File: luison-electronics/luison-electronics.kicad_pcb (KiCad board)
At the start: 2 copper layers, 120 x 80 mm, 28 parts, among them SW1 EECO_Micro-Dip_3500_B02, SW2 SW_Push, U1 YAAJ_DCDC_StepDown_LM2596

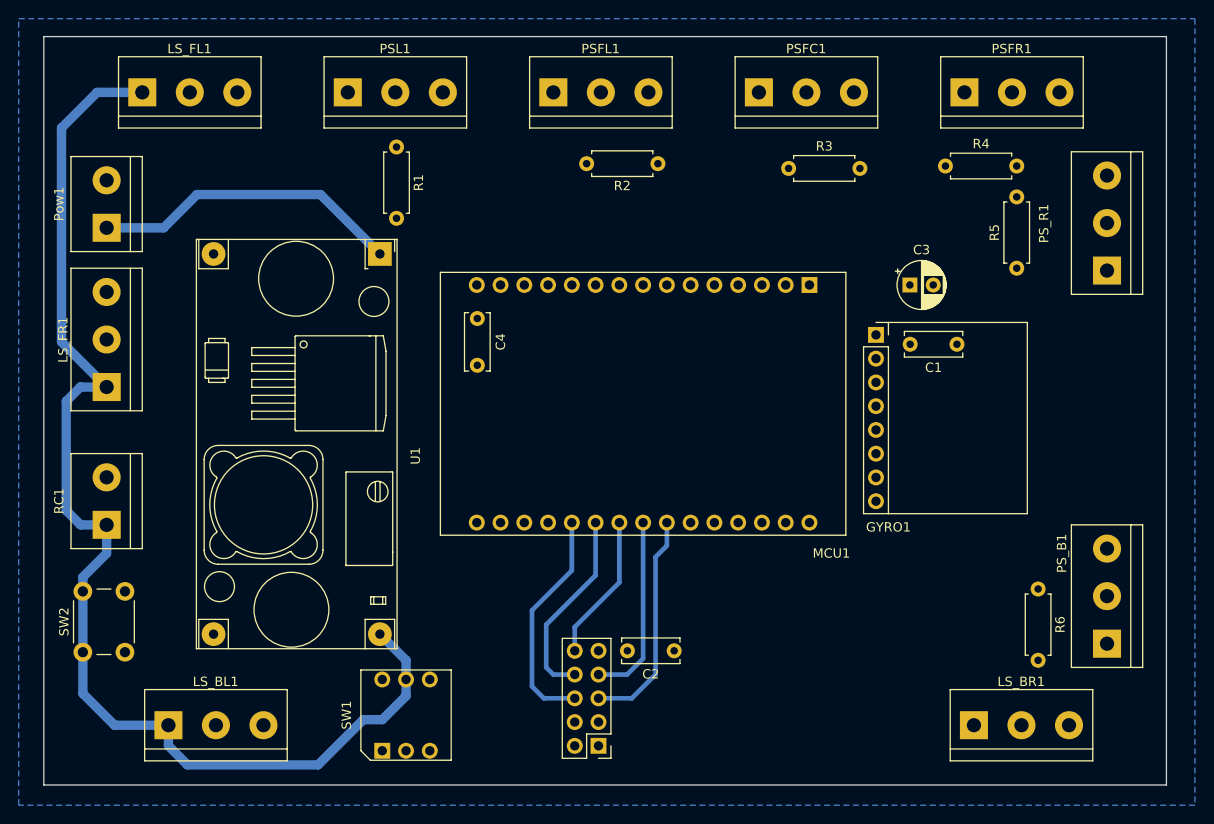
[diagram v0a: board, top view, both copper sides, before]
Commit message: Finish dual layer PCB and generate manufacture job files
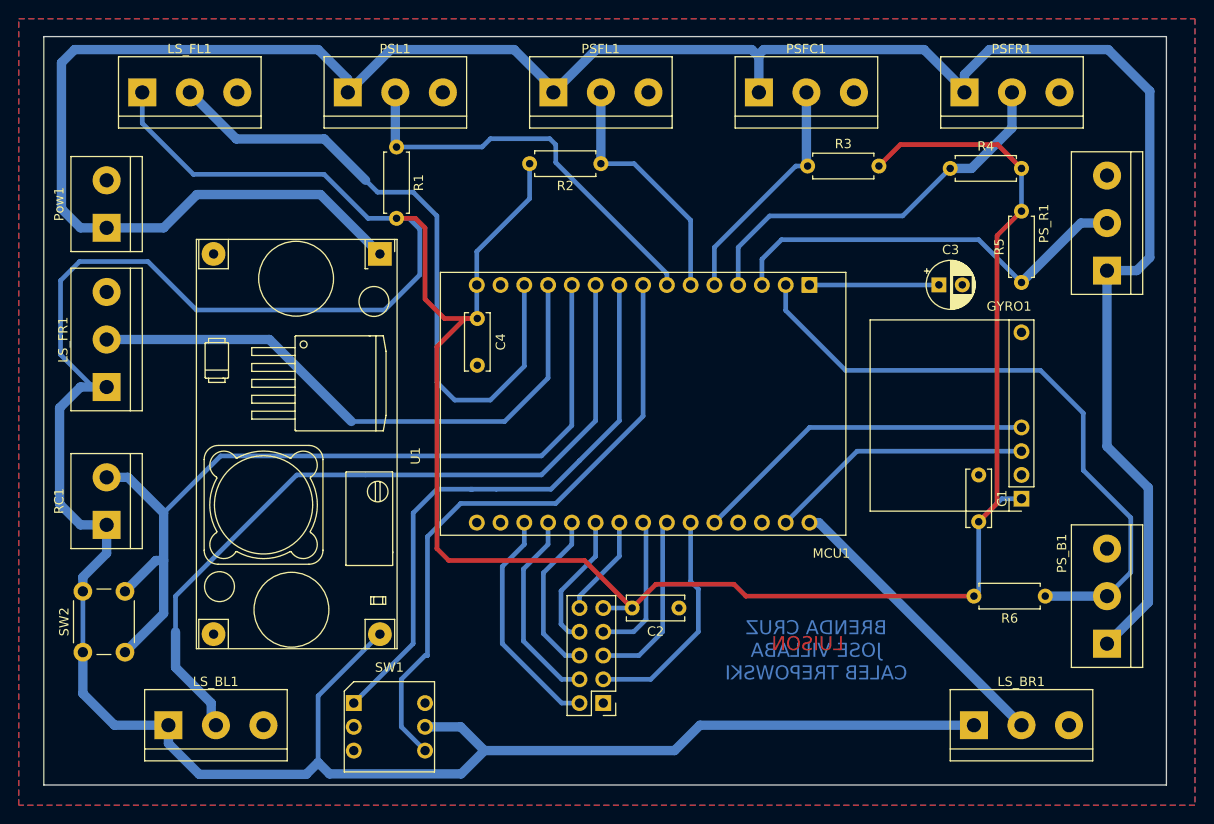
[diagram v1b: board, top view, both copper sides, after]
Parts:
- moved GYRO1 23.4 mm to (143.8, 122.9), turned to 180 degrees
- moved C1 14.2 mm to (139.2, 120.4), turned to -90 degrees
- moved R2 6.10 mm to (98.8, 87.1)
- moved SW1 5.94 mm to (72.4, 144.8), turned to -90 degrees
- moved C2 4.60 mm to (107.1, 134.6)
- moved MD1 4.60 mm to (99.1, 144.8)
- moved C3 3.11 mm to (134.9, 100.1)
- moved R3 2.05 mm to (120.9, 87.4)
- moved R5 1.61 mm to (143.8, 99.8)
- moved R6 1.08 mm to (146.3, 133.3), turned to 180 degrees
- moved R4 0.57 mm to (136.1, 87.6)
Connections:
- LS_BL1 pad 2: /GPIO14 -> /GPIO27
- LS_FR1 pad 2: /GPIO27 -> /GPIO12
- MCU1 pad 29: (no net) -> Net-(GYRO1-Pad3)
- Pow1 pad 2: (no net) -> GND
- RC1 pad 2: /GPIO12 -> /GPIO14
- SW2 pad 2: /GPIO12 -> /GPIO14
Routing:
- net +3.3V: track 130.4 -> 467.0 mm
- net +24V: track 33.3 -> 258.0 mm
- net /GPIO14: track 0.00 -> 92.3 mm
- net /GPIO27: track 0.00 -> 82.8 mm
- net /GPIO13: track 0.00 -> 70.0 mm
- net Net-(MCU1-Pad2): track 0.00 -> 68.4 mm
- net /GPIO25: track 0.00 -> 67.6 mm
- net /GPIO26: track 0.00 -> 63.8 mm
- net /GPIO12: track 0.00 -> 62.7 mm
- net Net-(MCU1-Pad3): track 0.00 -> 45.0 mm
- net Net-(MCU1-Pad7): track 0.00 -> 43.5 mm
- net Net-(MCU1-Pad4): track 0.00 -> 42.4 mm
- net Net-(GYRO1-Pad4): track 0.00 -> 37.0 mm
- net Net-(LS_BR1-Pad2): track 0.00 -> 31.6 mm
- net Net-(GYRO1-Pad3): track 0.00 -> 28.4 mm
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- added copper zone on F.Cu, net GND
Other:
- board text added: "BRENDA CRUZ JOSE VILLABA CALEB TREPOWSKI"
- board text added: "LUISON"

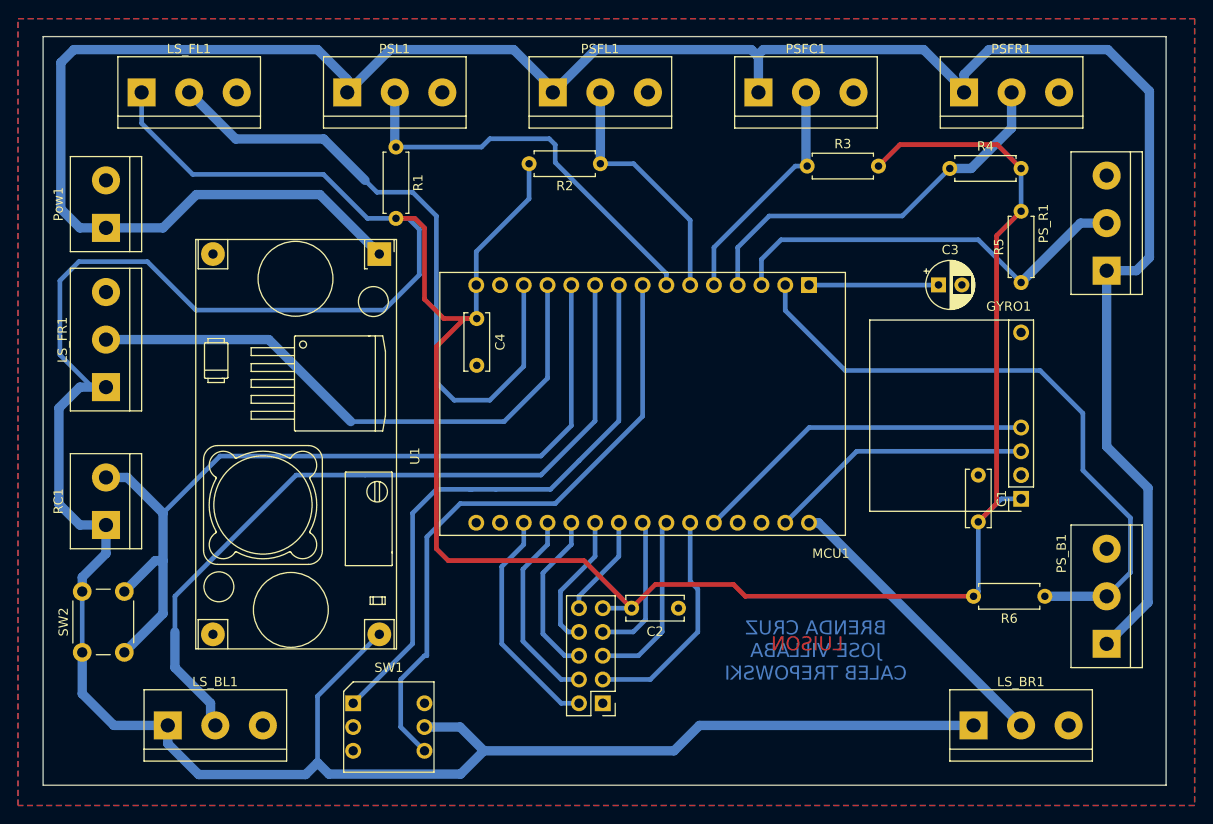
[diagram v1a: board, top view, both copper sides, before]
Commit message: Fix tracks, track widths and non-copper areas. Generate job files
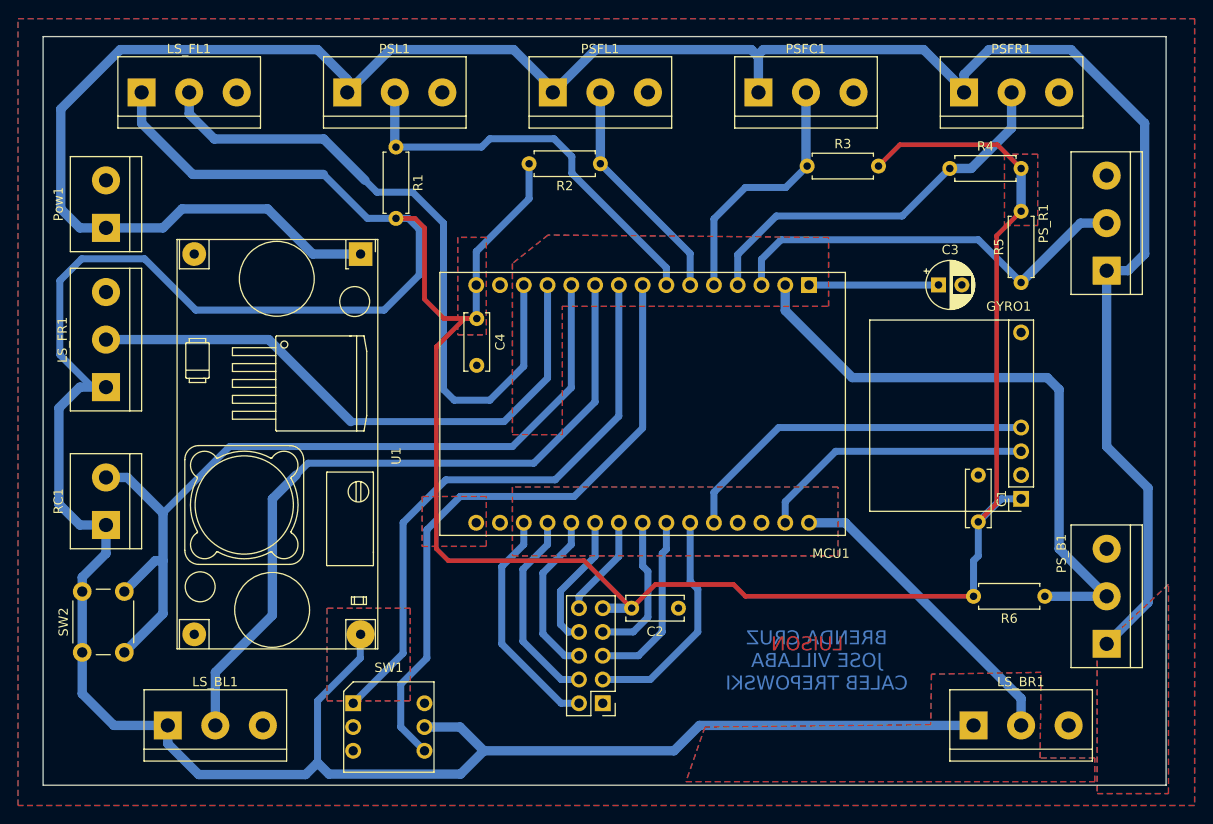
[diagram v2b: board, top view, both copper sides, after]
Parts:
- moved U1 2.00 mm to (73.2, 96.8)
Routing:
- net +24V: track 258.0 -> 248.6 mm
- net /GPIO27: track 82.8 -> 78.7 mm
- net /GPIO14: track 92.3 -> 89.9 mm
- net Net-(MCU1-Pad2): track 68.4 -> 66.3 mm
- net Net-(MCU1-Pad6): track 26.9 -> 24.8 mm
- net Net-(GYRO1-Pad4): track 37.0 -> 38.9 mm
- net Net-(MCU1-Pad5): track 25.5 -> 27.3 mm
- net Net-(LS_BR1-Pad2): track 31.6 -> 33.3 mm
- net /GPIO13: track 70.0 -> 71.3 mm
- net Net-(GYRO1-Pad3): track 28.4 -> 29.7 mm
- net /GPIO25: track 67.6 -> 68.7 mm
- net +3.3V: track 467.0 -> 466.4 mm
- net /GPIO26: track 63.8 -> 63.3 mm

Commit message: Add new symbols in schematic and new layout of pcb
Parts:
- added LS1: Line_Sensor, luison-electronics:JST_XH_B3B-XH-A_1x03_P2.50mm_Vertical, F.Cu at (236.0, 34.3)
- added LS2: Line_Sensor, luison-electronics:JST_XH_B3B-XH-A_1x03_P2.50mm_Vertical, F.Cu at (224.3, 34.3)
- added LS3: Line_Sensor, luison-electronics:JST_XH_B3B-XH-A_1x03_P2.50mm_Vertical, F.Cu at (242.8, 33.3)
- added LS4: Line_Sensor, luison-electronics:JST_XH_B3B-XH-A_1x03_P2.50mm_Vertical, F.Cu at (241.6, 79.0)
- added MCU2: ESP32-S2-DevKitC-1, luison-electronics:ESP32-S2-DevKitC-1, F.Cu at (233.4, 88.6)
- added PS1: Omron_E3Z-D62_2M, luison-electronics:JST_XH_B3B-XH-A_1x03_P2.50mm_Vertical, F.Cu at (281.9, 80.5)
- added PS2: Omron_E3Z-D62_2M, luison-electronics:JST_XH_B3B-XH-A_1x03_P2.50mm_Vertical, F.Cu at (298.5, 80.5)
- added PS3: Omron_E3Z-D62_2M, luison-electronics:JST_XH_B3B-XH-A_1x03_P2.50mm_Vertical, F.Cu at (208.5, 34.5)
- added PS4: Omron_E3Z-D62_2M, luison-electronics:JST_XH_B3B-XH-A_1x03_P2.50mm_Vertical, F.Cu at (229.4, 79.0)
- added PS5: Omron_E3Z-D62_2M, luison-electronics:JST_XH_B3B-XH-A_1x03_P2.50mm_Vertical, F.Cu at (205.3, 89.9)
- added PS6: Omron_E3Z-D62_2M, luison-electronics:JST_XH_B3B-XH-A_1x03_P2.50mm_Vertical, F.Cu at (298.5, 71.5)
- added REF**: MountingHole_3.2mm_M3, MountingHole:MountingHole_3.2mm_M3, F.Cu at (261.6, 27.7)
- added REF**: MountingHole_3.2mm_M3, MountingHole:MountingHole_3.2mm_M3, F.Cu at (261.6, 91.7)
- added REF**: MountingHole_3.2mm_M3, MountingHole:MountingHole_3.2mm_M3, F.Cu at (170.9, 91.7)
- added REF**: MountingHole_3.2mm_M3, MountingHole:MountingHole_3.2mm_M3, F.Cu at (170.9, 27.7)
- added SW3: EECO_Micro-Dip_3500_B02, luison-electronics:EECO Rotary Switch, F.Cu at (183.6, 84.6)
- moved C2 54.0 mm to (89.9, 83.4)
- moved GYRO1 54.0 mm to (126.5, 71.8)
- moved PS_B1 54.0 mm to (135.6, 87.2)
- moved SW2 54.0 mm to (26.2, 88.2)
- moved LS_FR1 54.0 mm to (28.7, 59.8)
- moved PS_R1 54.0 mm to (135.6, 47.4)
- moved Pow1 54.0 mm to (28.7, 42.8)
- moved R3 54.0 mm to (103.6, 36.2)
- moved R5 54.0 mm to (126.5, 48.6)
- moved C1 54.0 mm to (121.9, 69.2)
- moved C4 54.0 mm to (68.3, 52.5)
- moved LS_BL1 54.0 mm to (35.3, 96.0)
- moved LS_BR1 54.0 mm to (121.4, 96.0)
- moved LS_FL1 54.0 mm to (32.5, 28.3)
- moved MCU1 54.0 mm to (86.0, 61.6)
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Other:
- board size 120 x 80 mm -> 243.7 x 80 mm

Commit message: Add killlswitch library and layout pcb components
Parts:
- added D1: LED_RGB, LED_THT:LED_D5.0mm-4_RGB, F.Cu at (239.3, 105.4)
- added R7: 1k, Resistor_THT:R_Axial_DIN0207_L6.3mm_D2.5mm_P7.62mm_Horizontal, F.Cu at (224.0, 107.2)
- added R8: 1k, Resistor_THT:R_Axial_DIN0207_L6.3mm_D2.5mm_P7.62mm_Horizontal, F.Cu at (213.3, 111.2)
- added R9: 1k, Resistor_THT:R_Axial_DIN0207_L6.3mm_D2.5mm_P7.62mm_Horizontal, F.Cu at (213.3, 107.2)
- added U2: Robochallenge_KillSwitch, luison-electronics:Robochallenge_KillSwitch, F.Cu at (174.5, 71.9)
- moved PS1 86.2 mm to (195.8, 84.0), turned to 90 degrees
- moved PS2 64.5 mm to (244.6, 45.2), turned to 90 degrees
- moved MCU2 64.0 mm to (209.6, 29.2), turned to 0 degrees
- moved SW3 58.7 mm to (242.3, 86.9)
- moved PS6 56.1 mm to (246.1, 51.6), turned to -90 degrees
- moved PS5 48.8 mm to (246.1, 63.3), turned to -90 degrees
- moved LS2 47.7 mm to (195.6, 72.4), turned to 90 degrees
- moved LS3 47.5 mm to (195.6, 37.6), turned to 90 degrees
- moved LS4 45.8 mm to (244.6, 33.3), turned to 90 degrees
- moved LS1 43.0 mm to (195.6, 49.0), turned to 90 degrees
- moved PS3 29.0 mm to (195.8, 60.6), turned to 90 degrees
- moved REF** 17.5 mm to (188.5, 92.2)
- moved PS4 17.2 mm to (246.1, 75.0), turned to -90 degrees
- moved REF** 16.8 mm to (187.7, 27.7)
- moved REF** 5.59 mm to (256.0, 27.7)
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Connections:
- MCU2 pad 13: unconnected-(MCU2-Pad13) -> /KS_Start
- MCU2 pad 14: unconnected-(MCU2-Pad14) -> /KS_Em
- MCU2 pad 29: unconnected-(MCU2-Pad29) -> /LED_R
- MCU2 pad 30: unconnected-(MCU2-Pad30) -> /LED_G
- MCU2 pad 31: unconnected-(MCU2-Pad31) -> /LED_B
- MCU2 pad 32: unconnected-(MCU2-Pad32) -> /SW_P1
- MCU2 pad 33: unconnected-(MCU2-Pad33) -> /SW_P2
- MCU2 pad 34: unconnected-(MCU2-Pad34) -> /SW_P4
- MCU2 pad 35: unconnected-(MCU2-Pad35) -> /SW_P8
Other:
- board size 243.7 x 80 mm -> 241.2 x 80 mm

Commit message: Creacion de nueva placa
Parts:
- removed C1, C2, C4: 100nf, Capacitor_THT:C_Disc_D6.0mm_W2.5mm_P5.00mm
- removed C3: C, Capacitor_THT:CP_Radial_D5.0mm_P2.50mm
- removed D1: LED_RGB, LED_THT:LED_D5.0mm-4_RGB
- removed GYRO1: MPU-6050 Breakout Board, keilev_Library:MPU6050 Breakout Board
- removed LS_BL1, LS_BR1, LS_FL1, LS_FR1: Line_Sensor, TerminalBlock:TerminalBlock_bornier-3_P5.08mm
- removed MCU1: ESP32-Node32s, luison-electronics:ESP32-Node32s
- removed MD1: H-Bridge_Driver, Connector_PinHeader_2.54mm:PinHeader_2x05_P2.54mm_Vertical
- removed PSFC1, PSFL1, PSFR1, PSL1, PS_B1, PS_R1: Omron_E3Z-D62_2M, TerminalBlock:TerminalBlock_bornier-3_P5.08mm
- removed Pow1: Power_Supply, TerminalBlock:TerminalBlock_bornier-2_P5.08mm
- removed R1, R2, R3, R4, R5, R6: 1Meg, Resistor_THT:R_Axial_DIN0207_L6.3mm_D2.5mm_P7.62mm_Horizontal
- removed R7, R8, R9: 1k, Resistor_THT:R_Axial_DIN0207_L6.3mm_D2.5mm_P7.62mm_Horizontal
- removed RC1: Remote_Control_Module, TerminalBlock:TerminalBlock_bornier-2_P5.08mm
- removed SW1: EECO_Micro-Dip_3500_B02, luison-electronics:EECO Rotary Switch
- removed SW2: SW_Push, Button_Switch_THT:SW_PUSH_6mm
- removed U1: YAAJ_DCDC_StepDown_LM2596, luison-electronics:YAAJ_DCDC_StepDown_LM2596
- added ?: , , F.Cu at (170.8, 104.8)
- added ?: , , F.Cu at (179.1, 74.9)
- added ?: , , F.Cu at (138.4, 74.9)
- added ?: , , F.Cu at (123.6, 90.8)
- added GYRO2: MPU-6050 Breakout Board, luison-electronics:MPU6050 Breakout Board, F.Cu at (117.4, 82.5)
- added PS7: conector_driver, luison-electronics:JST_XH_B3B-XH-A_1x03_P2.50mm_Vertical, F.Cu at (148.0, 108.6)
- added PS8: alimentacion_driver, luison-electronics:JST_XH_B3B-XH-A_1x03_P2.50mm_Vertical, F.Cu at (115.4, 105.2)
- added PS9: alimentacion_driver, luison-electronics:JST_XH_B3B-XH-A_1x03_P2.50mm_Vertical, F.Cu at (115.3, 93.3)
- added REF**: custom_via, luison-electronics:custom_via, F.Cu at (141.6, 113.0)
- moved REF** 166.6 mm to (114.9, 116.2), turned to 0 degrees
- moved MCU2 110.6 mm to (127.0, 102.8), turned to 90 degrees
- moved LS4 107.9 mm to (143.5, 71.0), turned to 180 degrees
- moved PS2 94.4 mm to (175.8, 109.9), turned to 180 degrees
- moved LS1 92.3 mm to (125.1, 108.6), turned to 0 degrees
- moved SW3 87.2 mm to (156.2, 73.0), turned to 90 degrees
- moved PS4 79.9 mm to (166.4, 70.9), turned to 180 degrees
- moved REF** 79.2 mm to (114.9, 59.1), turned to 0 degrees
- moved PS5 73.7 mm to (172.7, 69.8), turned to 0 degrees
- moved REF** 72.7 mm to (190.5, 62.2), turned to 0 degrees
- moved LS3 71.8 mm to (132.0, 71.0), turned to 180 degrees
- moved LS2 69.2 mm to (136.6, 108.6), turned to 0 degrees
- moved PS6 60.1 mm to (189.2, 70.9), turned to 180 degrees
- moved PS3 49.8 mm to (182.2, 108.6), turned to 0 degrees
- moved U2 47.3 mm to (154.9, 114.9), turned to -90 degrees
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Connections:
- MCU2 pad 10: /TX1_MD -> /RX1_MD
- MCU2 pad 11: /RX1_MD -> /KS_START
- MCU2 pad 12: /SDA -> unconnected-(MCU2-IO8/ADC-Pad12)
- MCU2 pad 13: /KS_Start -> unconnected-(MCU2-IO3/ADC-Pad13)
- MCU2 pad 14: /KS_Em -> unconnected-(MCU2-I46-Pad14)
- MCU2 pad 15: /SCL -> /PS_FL
- MCU2 pad 17: /PS_FR -> unconnected-(MCU2-IO11/ADC-Pad17)
- MCU2 pad 18: /PS_FC -> unconnected-(MCU2-IO12/ADC-Pad18)
- MCU2 pad 19: /PS_FL -> /PS_FC
- MCU2 pad 20: unconnected-(MCU2-Pad20) -> /PS_FR
- MCU2 pad 24: unconnected-(MCU2-Pad24) -> /LS_FR
- MCU2 pad 25: unconnected-(MCU2-Pad25) -> /SDA
- MCU2 pad 26: /LS_BR -> /SCL
- MCU2 pad 27: /LS_BL -> unconnected-(MCU2-IO2/ADC-Pad27)
- MCU2 pad 28: unconnected-(MCU2-Pad28) -> /LS_BR
- MCU2 pad 29: /LED_R -> unconnected-(MCU2-IO41-Pad29)
- MCU2 pad 3: unconnected-(MCU2-Pad3) -> /LS_FL
- MCU2 pad 30: /LED_G -> /SW_P2
- MCU2 pad 31: /LED_B -> /SW_P8
- MCU2 pad 32: /SW_P1 -> unconnected-(MCU2-IO38-Pad32)
- MCU2 pad 33: /SW_P2 -> /SW_P4
- MCU2 pad 34: /SW_P4 -> /SW_P1
- MCU2 pad 35: /SW_P8 -> unconnected-(MCU2-IO35-Pad35)
- MCU2 pad 37: unconnected-(MCU2-Pad37) -> /PS_L
- MCU2 pad 38: /PS_R -> unconnected-(MCU2-IO34-Pad38)
- MCU2 pad 39: /PS_B -> unconnected-(MCU2-IO33-Pad39)
- MCU2 pad 4: unconnected-(MCU2-Pad4) -> /4
- MCU2 pad 40: /PS_L -> unconnected-(MCU2-IO21-Pad40)
- MCU2 pad 41: unconnected-(MCU2-Pad41) -> /PS_B
- MCU2 pad 42: unconnected-(MCU2-Pad42) -> /PS_R
- MCU2 pad 5: /LS_FR -> /LS_BL
- MCU2 pad 6: /LS_FL -> /6
- MCU2 pad 7: unconnected-(MCU2-Pad7) -> /7
- MCU2 pad 8: unconnected-(MCU2-Pad8) -> /TX1_MD
- MCU2 pad 9: unconnected-(MCU2-Pad9) -> /KS_EM
- U2 pad 2: /KS_Start -> /KS_START
- U2 pad 3: /KS_Em -> /KS_EM
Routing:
- net +3.3V: track 466.4 -> 178.5 mm
- net /GPIO14: track 89.9 -> 0.00 mm
- net /GPIO27: track 78.7 -> 0.00 mm
- net /GPIO13: track 71.3 -> 0.00 mm
- net /GPIO25: track 68.7 -> 0.00 mm
- net +5V: track 0.00 -> 68.2 mm
- net Net-(MCU1-Pad2): track 66.3 -> 0.00 mm
- net +24V: track 248.6 -> 184.4 mm
- net /GPIO26: track 63.3 -> 0.00 mm
- net /GPIO12: track 62.7 -> 0.00 mm
- net Net-(MCU1-Pad3): track 45.0 -> 0.00 mm
- net Net-(MCU1-Pad7): track 43.8 -> 0.00 mm
- net Net-(MCU1-Pad4): track 41.9 -> 0.00 mm
- net Net-(GYRO1-Pad4): track 38.9 -> 0.00 mm
- net /7: track 0.00 -> 34.2 mm
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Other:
- board size 241.2 x 80 mm -> 83.2 x 64.8 mm
- board text added: "++G5"
- board text added: "764"
- board text added: "G EM S +"
- board text added: "LSBL"
- board text added: "LSBR"
- board text added: "LSFL"
- board text added: "LSFR"
- board text added: "PSB"
- board text added: "PSFC"
- board text added: "PSFL"
- board text added: "PSFR"
- board text added: "PSL"
- board text added: "PSR"
- board text removed: "BRENDA CRUZ JOSE VILLABA CALEB TREPOWSKI"
